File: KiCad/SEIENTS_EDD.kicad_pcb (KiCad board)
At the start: 2 copper layers, 130.1 x 90 mm, 99 parts, among them IC1 A3144EUA, J1 Conn_01x02_Pin, J201 Screw_Terminal_01x04, J3 Screw_Terminal_01x05, J4 Screw_Terminal_01x02, J7 DE9_Socket, J8 DE9_Pins, M4 Motor_DC, M5 Motor_DC, M6 Motor_DC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

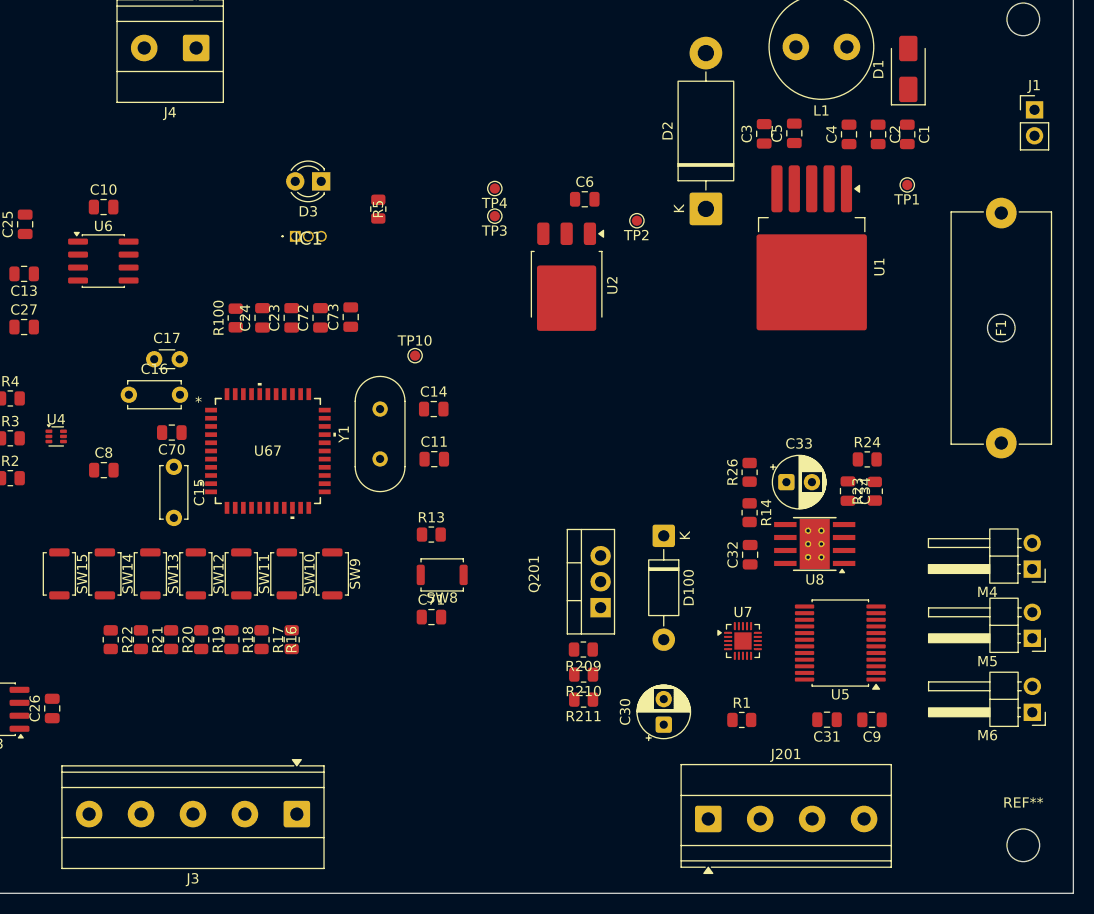
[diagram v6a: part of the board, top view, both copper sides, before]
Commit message: FootPrints Canviats
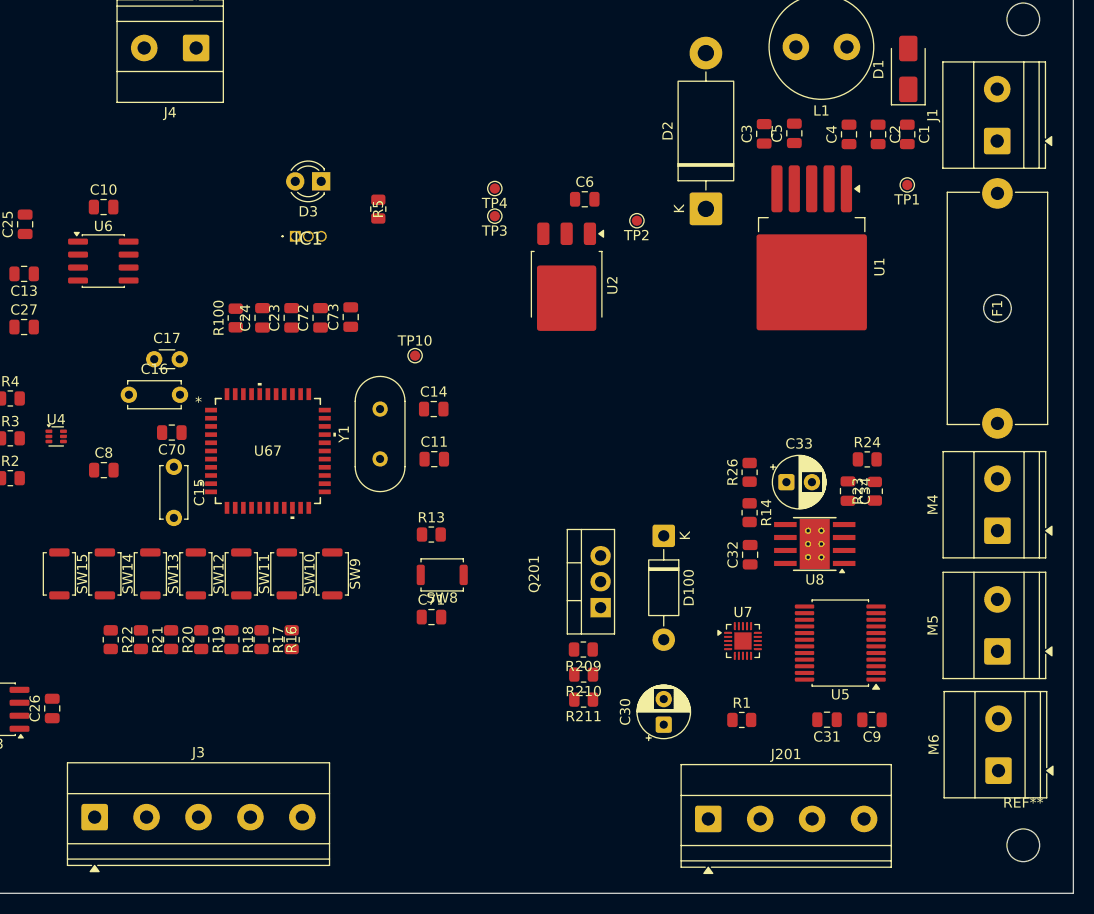
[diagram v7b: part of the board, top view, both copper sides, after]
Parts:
- J1: footprint Connector_PinHeader_2.54mm:PinHeader_1x02_P2.54mm_Vertical -> TerminalBlock_Phoenix:TerminalBlock_Phoenix_MKDS-1,5-2-5.08_1x02_P5.08mm_Horizontal
- M4, M5, M6: footprint Connector_PinHeader_2.54mm:PinHeader_1x02_P2.54mm_Horizontal -> TerminalBlock_Phoenix:TerminalBlock_Phoenix_MKDS-1,5-2-5.08_1x02_P5.08mm_Horizontal
- moved J3 19.8 mm to (124.2, 137.6), turned to 0 degrees
- moved M6 6.60 mm to (212.7, 133.0), turned to 90 degrees
- moved M4 5.06 mm to (212.6, 109.5), turned to 90 degrees
- moved J1 4.76 mm to (212.6, 71.4), turned to 90 degrees
- moved M5 3.64 mm to (212.6, 121.3), turned to 90 degrees
- moved F1 1.96 mm to (212.6, 99.0)

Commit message: Rounting
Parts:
- moved R18 39.4 mm to (173.5, 103.8), turned to 180 degrees
- moved R17 38.2 mm to (173.5, 100.8), turned to 180 degrees
- moved R16 37.4 mm to (173.5, 98.0), turned to 180 degrees
- moved SW11 29.3 mm to (166.4, 104.5), turned to 0 degrees
- moved R24 28.8 mm to (187.1, 128.4)
- moved SW10 27.1 mm to (166.4, 100.1), turned to 0 degrees
- moved SW9 26.2 mm to (166.4, 95.7), turned to 0 degrees
- moved R4 4.24 mm to (116.0, 100.8)
- moved TP4 3.20 mm to (163.2, 79.2)
- moved R3 2.91 mm to (115.9, 97.6)
- moved TP3 2.30 mm to (163.2, 76.5)
- moved R1 2.05 mm to (187.1, 126.0)
- moved R19 1.78 mm to (136.3, 120.8), turned to 90 degrees
- moved R20 1.77 mm to (133.4, 120.8), turned to 90 degrees
- moved R21 1.61 mm to (130.3, 120.7), turned to 90 degrees
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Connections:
- U7 pad 11: ALT_IN2 -> unconnected-(U7-PB3-Pad11)
- U7 pad 12: ALT_IN1 -> unconnected-(U7-PB2-Pad12)
- U7 pad 13: REC_IN2 -> REC_IN1
- U7 pad 14: REC_IN1 -> REC_IN2
- U7 pad 15: unconnected-(U7-PC0-Pad15) -> ALT_IN2
- U7 pad 16: unconnected-(U7-PC1-Pad16) -> ALT_IN1
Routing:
- net +3.3V: track 0.00 -> 519.9 mm, vias 0 -> 4
- net +5V: track 0.16 -> 235.2 mm, vias 0 -> 3
- net VBAT: track 0.00 -> 185.8 mm
- net GND: track 0.00 -> 153.2 mm, vias 0 -> 48
- net MCU_SDA: track 0.00 -> 148.8 mm, vias 0 -> 6
- net MCU_SCL: track 0.00 -> 109.7 mm, vias 0 -> 4
- net POS_IN2: track 0.00 -> 77.6 mm, vias 0 -> 4
- net POS_PWM: track 0.00 -> 72.3 mm, vias 0 -> 2
- net POS_IN1: track 0.00 -> 72.1 mm, vias 0 -> 3
- net T_SEIENTS: track 0.00 -> 71.5 mm, vias 0 -> 2
- net REC_IN2: track 0.00 -> 71.0 mm, vias 0 -> 2
- net REC_IN1: track 0.00 -> 70.5 mm, vias 0 -> 2
- net REC_PWM: track 0.00 -> 69.1 mm, vias 0 -> 3
- net Net-(J3-Pin_1): track 0.00 -> 65.0 mm, vias 0 -> 4
- net CALEFACCIÓ: track 0.00 -> 51.9 mm, vias 0 -> 2
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- added copper zone on B.Cu, net GND
